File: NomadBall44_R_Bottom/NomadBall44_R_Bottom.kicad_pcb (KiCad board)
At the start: 2 copper layers, 147.4 x 96.5 mm, 56 parts, among them SW1 SW_Push, SW10 SW_Push, SW11 SW_Push, SW12 SW_Push, SW13 SW_Push, SW14 SW_Push, SW15 SW_Push, SW16 SW_Push, SW17 SW_Push, SW18 SW_Push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

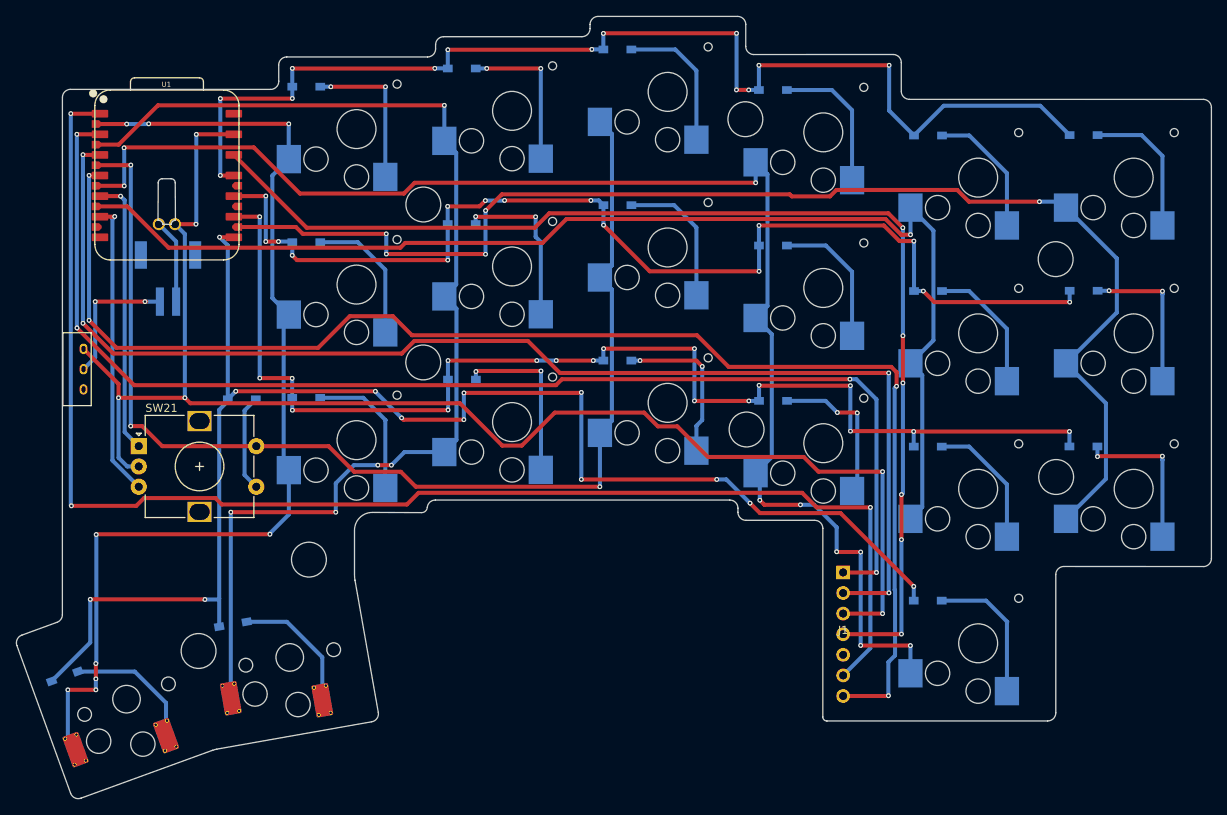
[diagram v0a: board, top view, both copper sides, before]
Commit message: ダイオードとキースイッチのフットプリントを削除
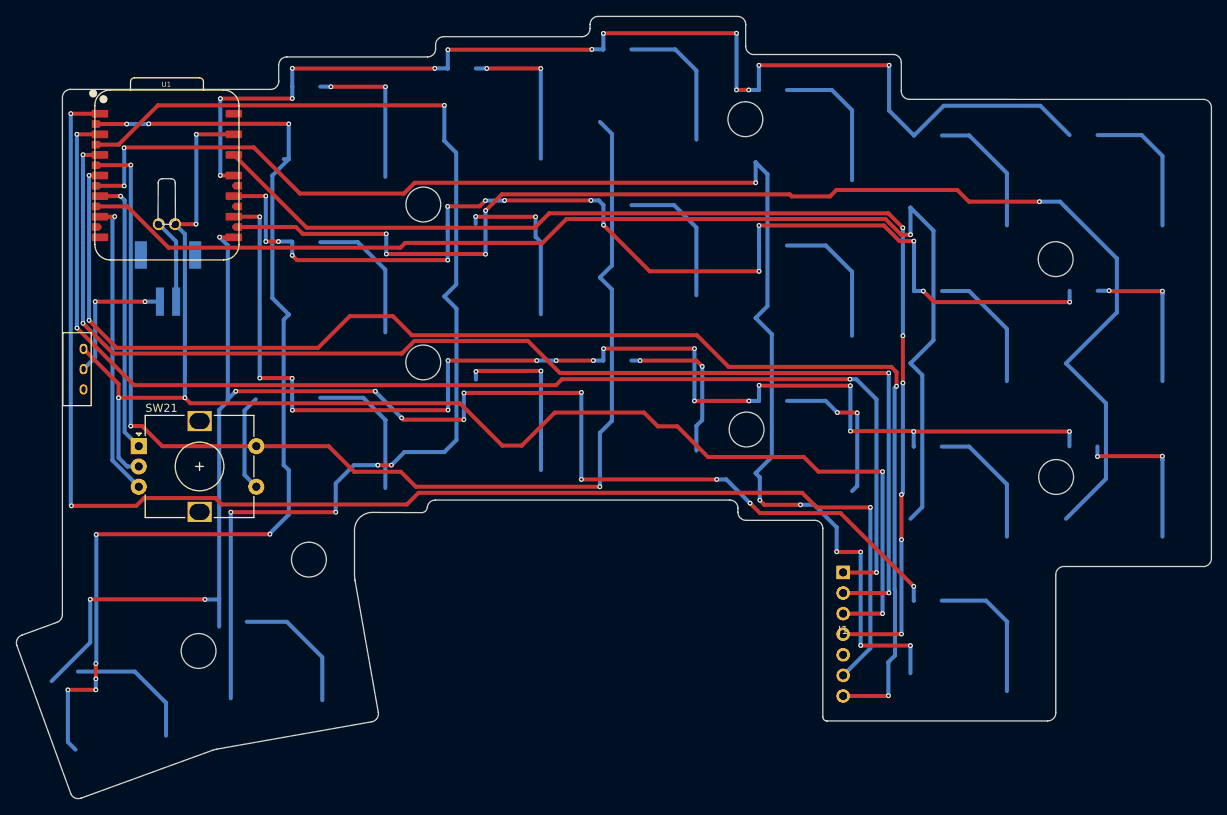
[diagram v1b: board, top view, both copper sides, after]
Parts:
- removed D1, D10, D11, D12, D13, D14, D15, D16, D17, D18, D19, D2, D20, D21, D22, D3, D4, D5, D6, D7, D8, D9: D, NomadBall44:Diode_SMD
- removed SW1, SW10, SW11, SW12, SW13, SW14, SW15, SW16, SW17, SW18, SW2, SW22, SW3, SW4, SW5, SW6, SW7, SW8, SW9: SW_Push, NomadBall44:Choc_v2_Hotswap_1u
- removed SW19, SW20: SW_Push, NomadBall44:Kailh_Choc_V1_Hotswap_thin_via

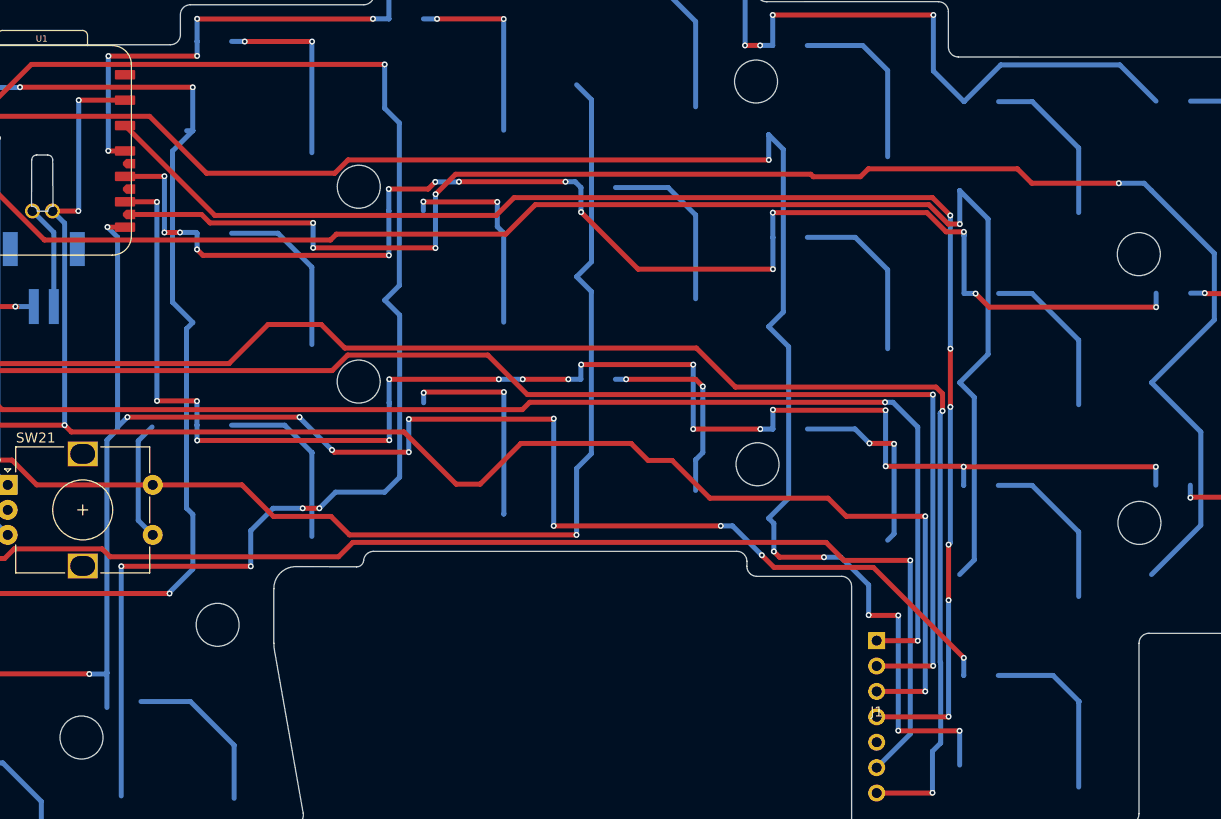
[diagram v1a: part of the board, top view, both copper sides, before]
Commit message: ネジ用ホールを設定
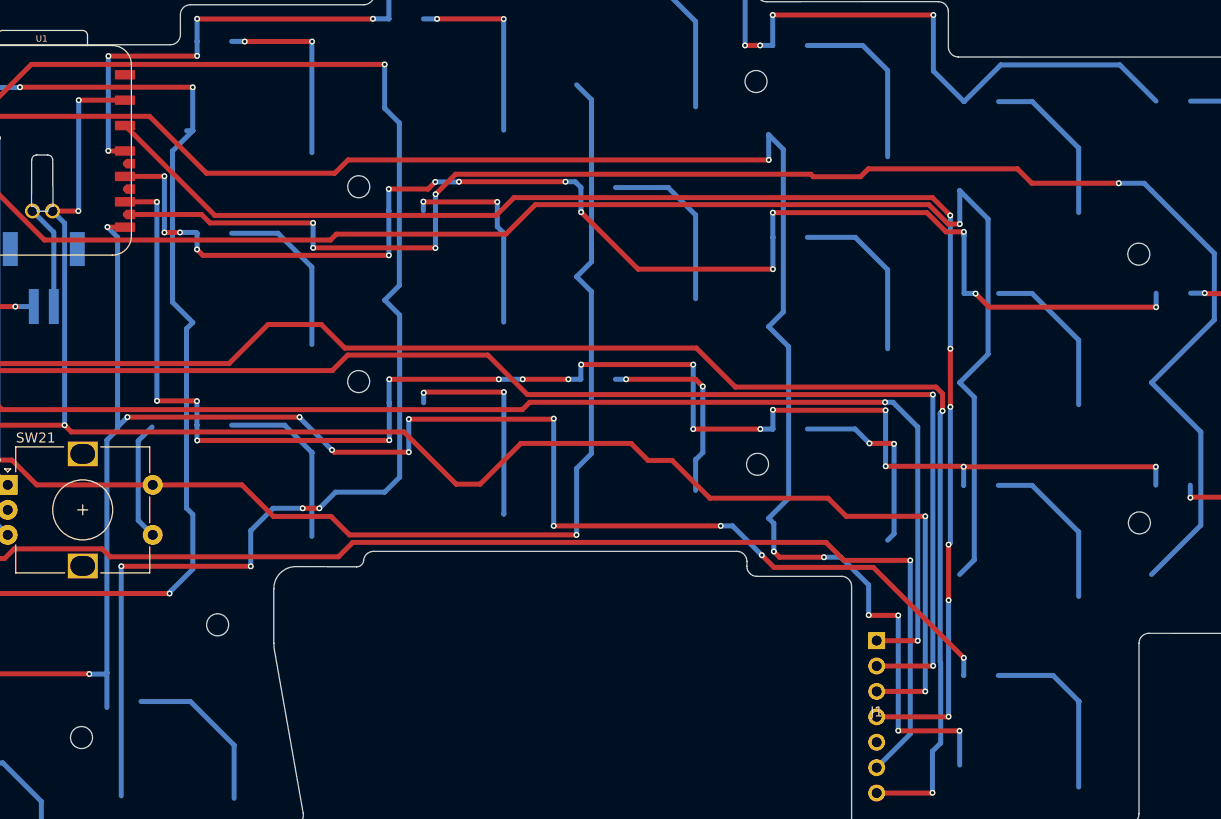
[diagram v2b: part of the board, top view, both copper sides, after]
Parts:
- REF** (x8): value MountingHole_4.3mm_M4 -> Val**; footprint MountingHole:MountingHole_4.3mm_M4 -> NomadBall44:m2_Screw_Hole_EdgeCuts

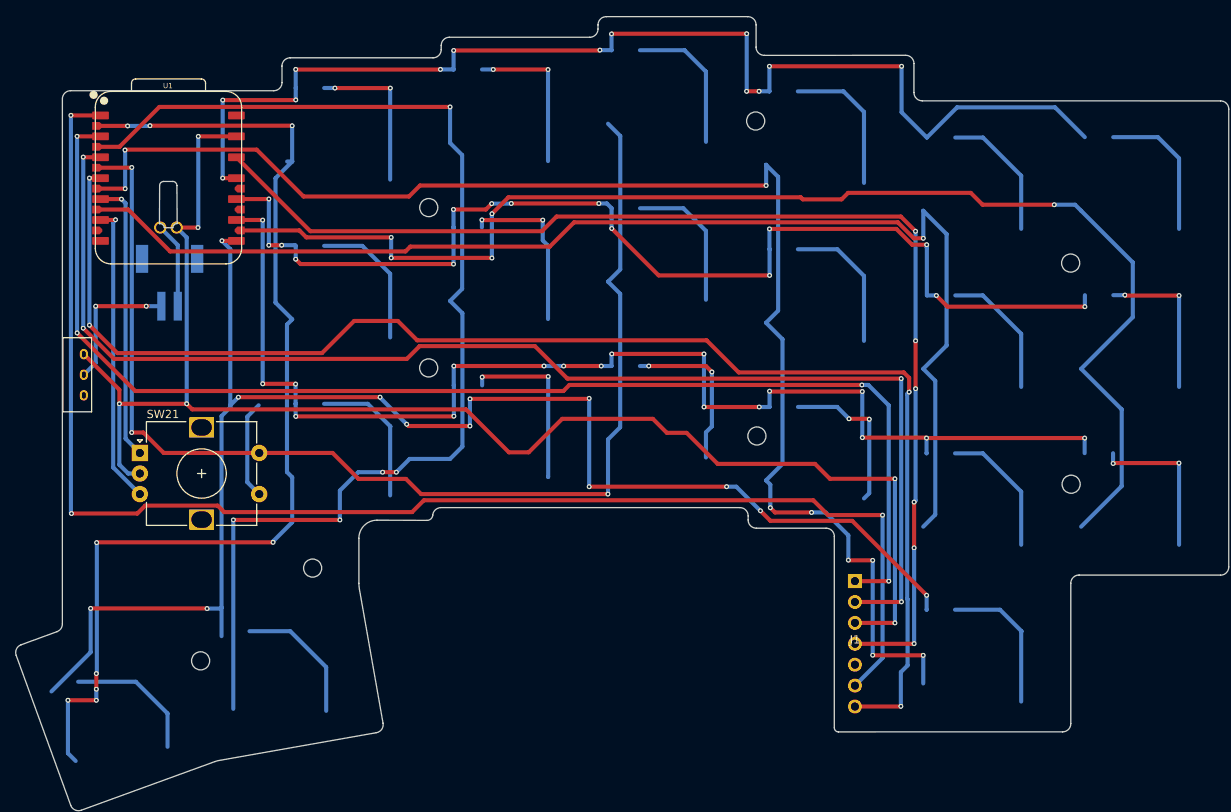
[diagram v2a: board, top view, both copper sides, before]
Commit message: 配線を削除
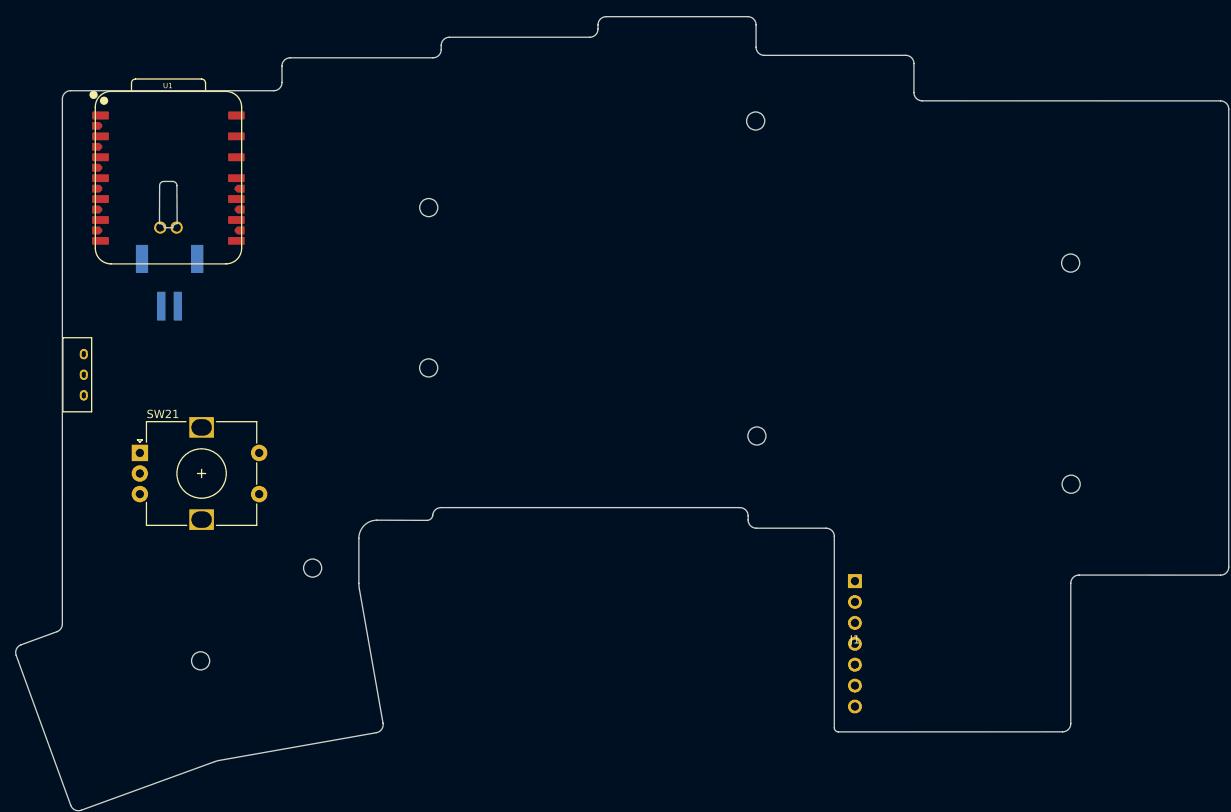
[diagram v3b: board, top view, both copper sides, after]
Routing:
- net Row3: track 186.4 -> 0.00 mm, vias 13 -> 0
- net GND: track 182.4 -> 0.23 mm, vias 6 -> 0
- net SDIO: track 174.7 -> 0.00 mm, vias 3 -> 0
- net Col3: track 174.5 -> 0.37 mm, vias 9 -> 0
- net MOTION: track 170.7 -> 0.00 mm, vias 4 -> 0
- net Col5: track 160.3 -> 0.00 mm, vias 5 -> 0
- net CS: track 158.9 -> 0.00 mm, vias 4 -> 0
- net SCLK: track 155.1 -> 0.01 mm, vias 4 -> 0
- net Row2: track 152.2 -> 0.00 mm, vias 18 -> 0
- net Col4: track 150.0 -> 0.00 mm, vias 1 -> 0
- net 3.3V: track 145.1 -> 0.00 mm, vias 6 -> 0
- net Col2: track 144.8 -> 0.00 mm, vias 3 -> 0
- net Col1: track 144.5 -> 0.00 mm, vias 5 -> 0
- net Row0: track 143.9 -> 0.00 mm, vias 13 -> 0
- net Row1: track 137.2 -> 0.00 mm, vias 15 -> 0
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
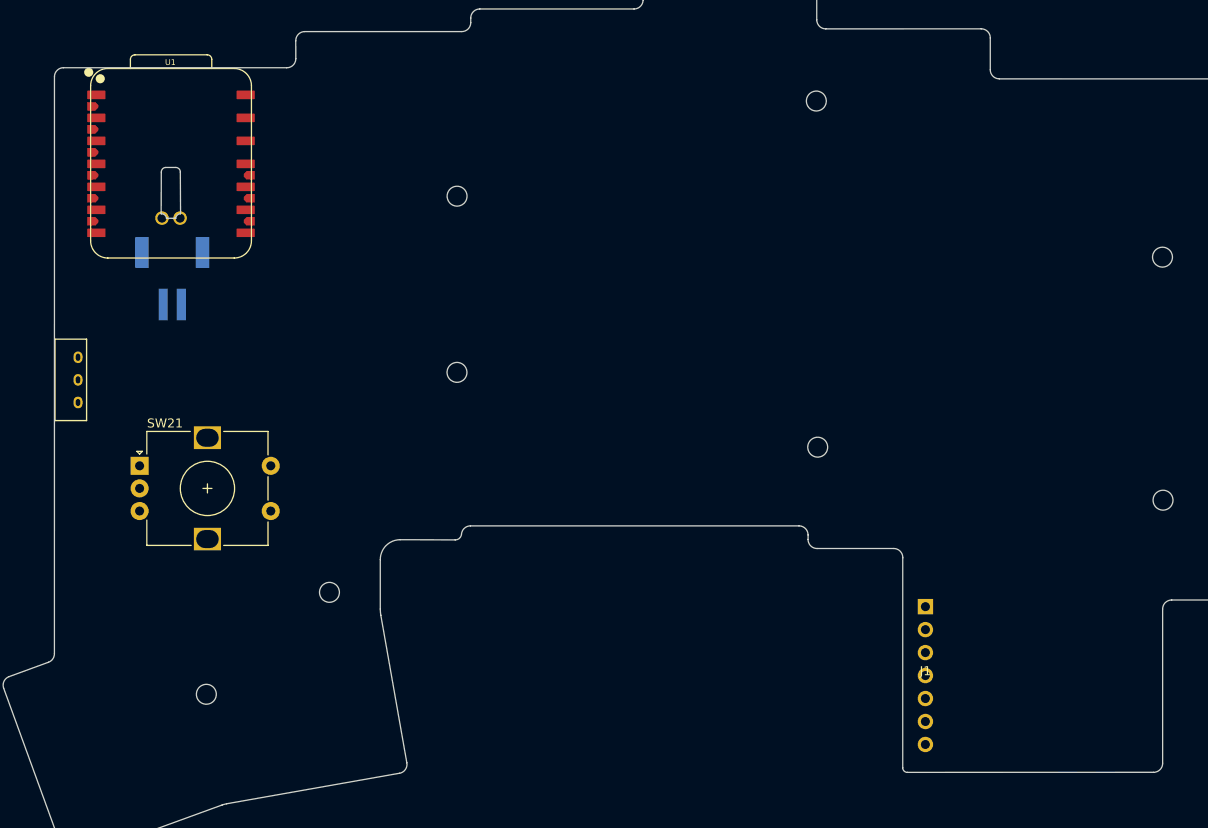
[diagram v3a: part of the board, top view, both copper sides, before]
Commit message: 不要な配線を削除
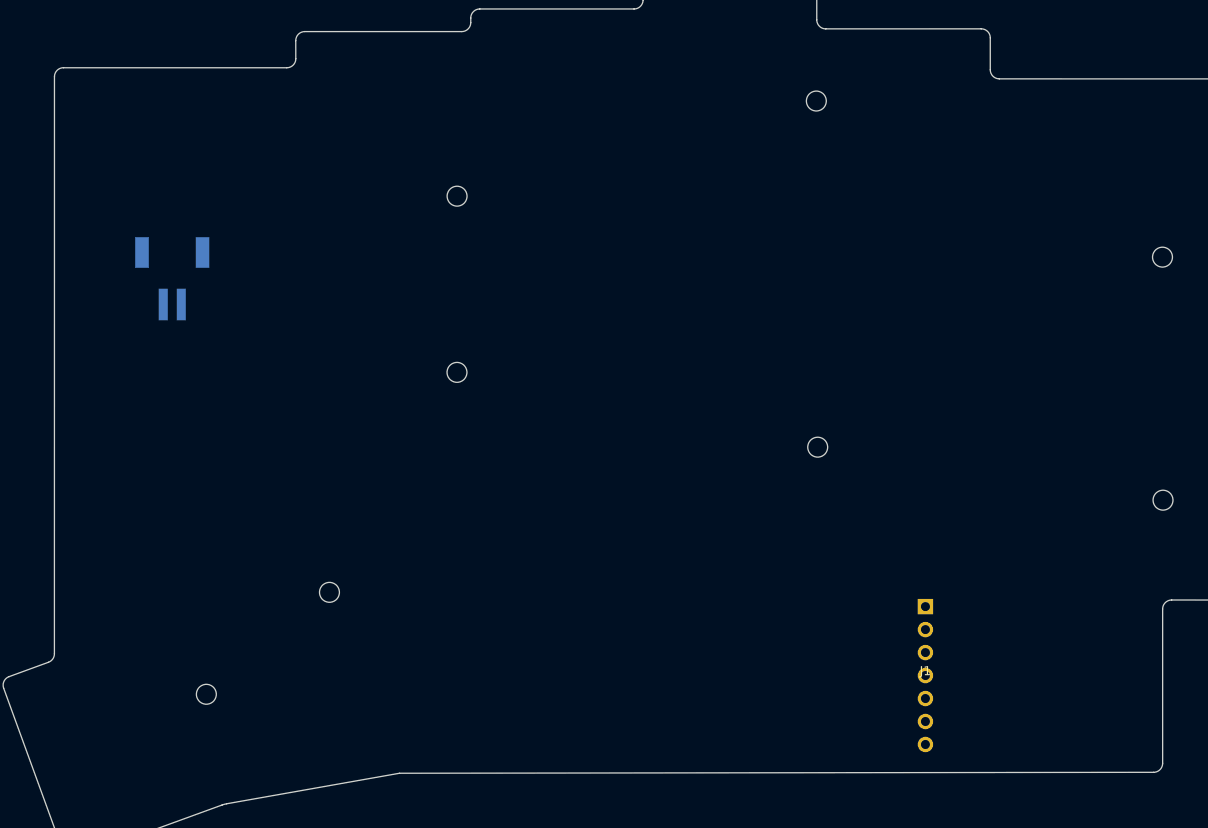
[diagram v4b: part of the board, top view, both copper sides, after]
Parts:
- removed SW21: RotaryEncoder_Switch, Rotary_Encoder:RotaryEncoder_Alps_EC12E-Switch_Vertical_H20mm
- removed SW23: SW_SPDT, NomadBall44:TGSW_MSK-12D19
- removed U1: XIAO-nRF52840-Plus-SMD, NomadBall44:XIAO-nRF52840-Plus
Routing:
- net Bat: track 0.95 -> 0.00 mm
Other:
- outline, holes or cut-outs redrawn

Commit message: PHコネクタとバッテリー用のエリアを作成
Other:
- board size 147.4 x 96.5 mm -> 330.3 x 100.7 mm

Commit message: ネジ穴を一つ追加
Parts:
- added REF**: Val**, NomadBall44:m2_Screw_Hole_EdgeCuts, F.Cu at (186.3, 108.4)
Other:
- board size 330.3 x 100.7 mm -> 527.6 x 105.9 mm
